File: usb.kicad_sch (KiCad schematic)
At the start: 67 parts, among them J3 USB-C_GCT_USB4105-GF-A, Q2 BC817-25W, U11 AP22652W6, U2 FT4232H_VQFN, U4 AP62301_TSOT, U5 TPD4E05U06QDQARQ1, U8 AP62301_TSOT, Y1 Resonator_12MHz_ABM8G

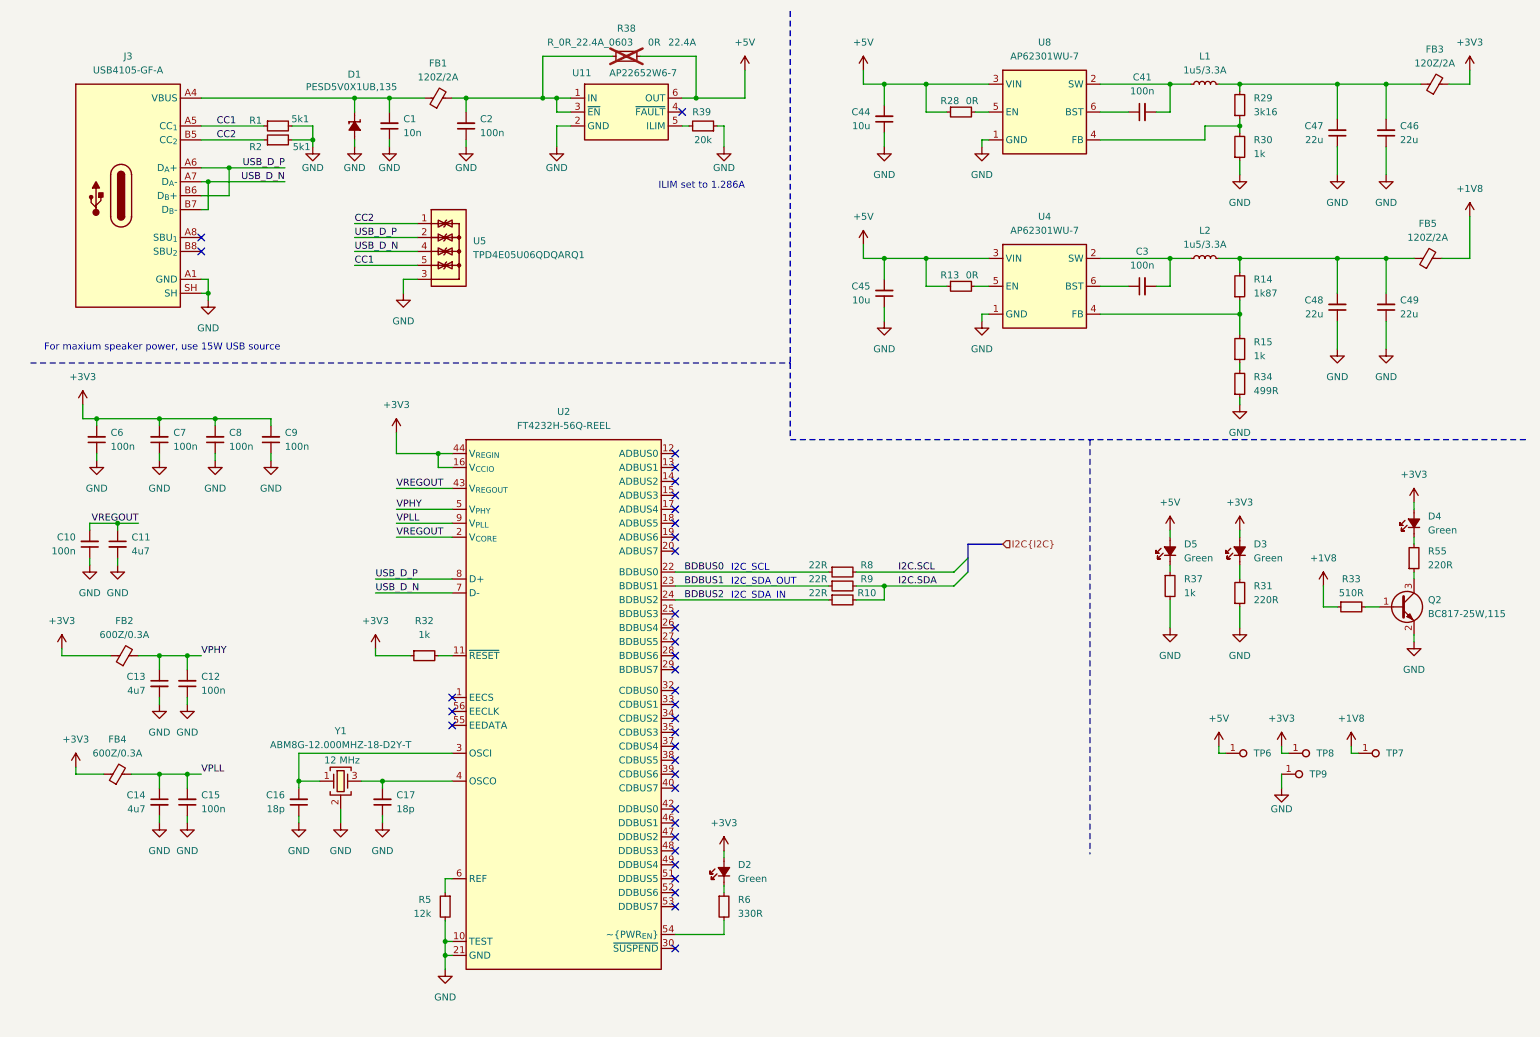
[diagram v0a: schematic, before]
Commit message: [#71555] Add new root sheet structure
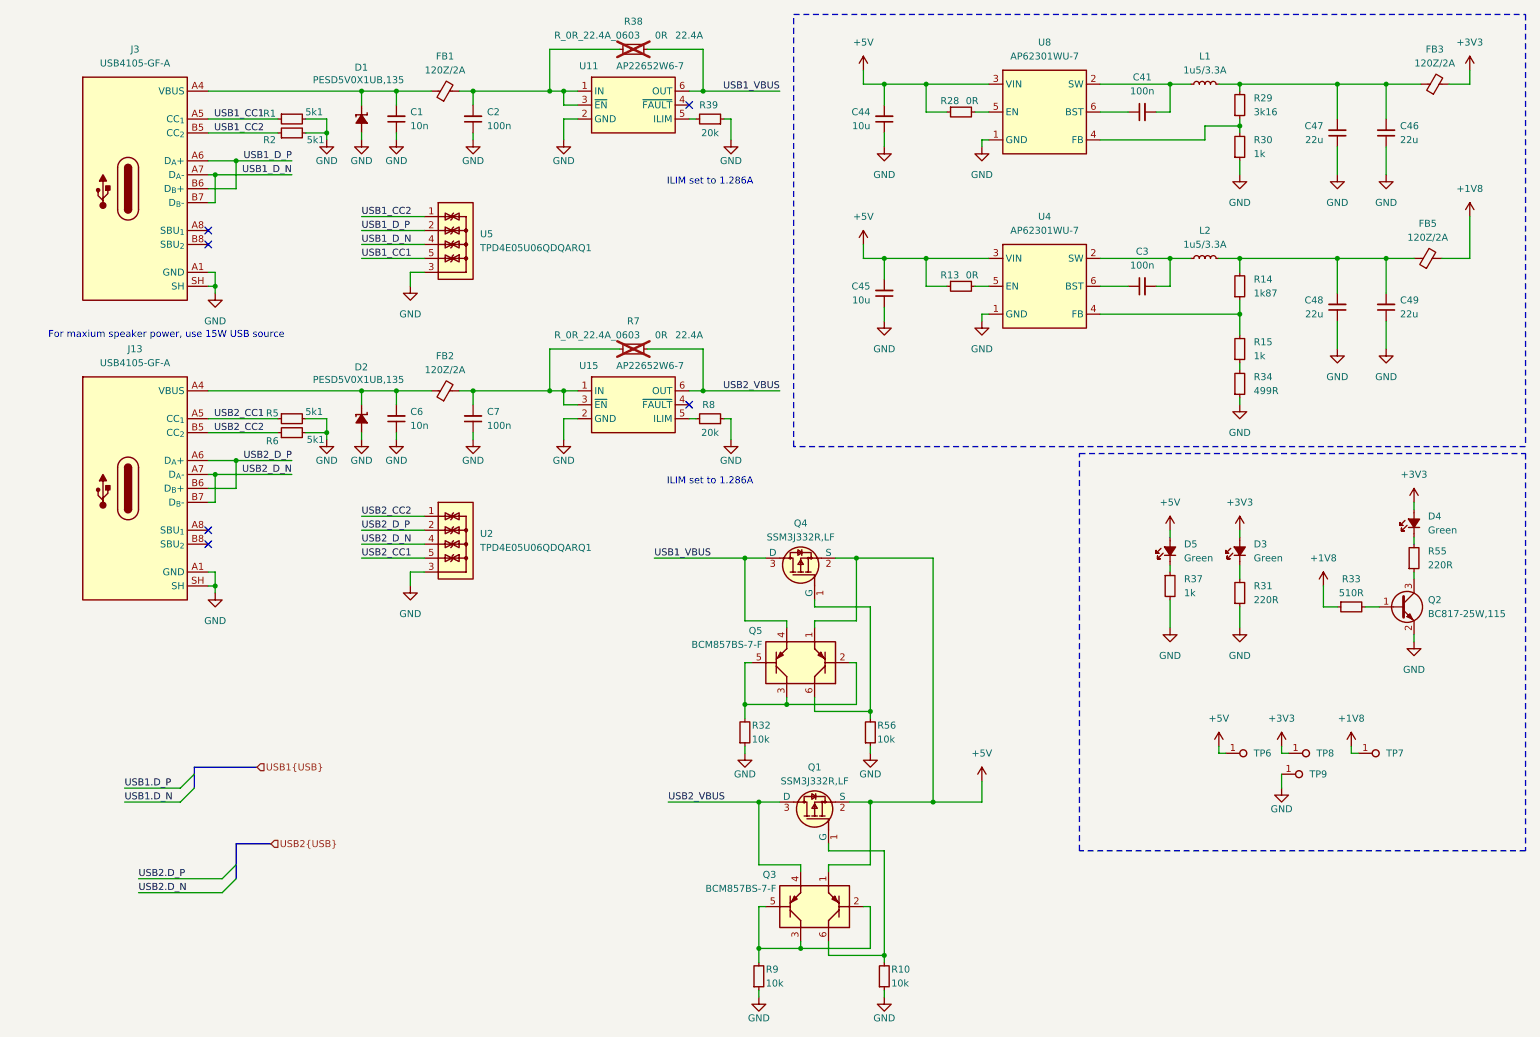
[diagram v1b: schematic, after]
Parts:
- removed C10, C12, C15, C6, C8, C9: C_100n_0402, antmicro-footprints:C_0402_1005Metric, symbol antmicroCapacitors0402:C_100n_0402
- removed C11, C13, C14: C_4u7_0402, antmicro-footprints:C_0402_1005Metric, symbol antmicroCapacitors0402:C_4u7_0402
- removed C16, C17: C_18p_0402, antmicro-footprints:C_0402_1005Metric, symbol antmicroCapacitors0402:C_18p_0402
- removed D2: LED_G_0402_VLMTG1500-GS08, antmicro-footprints:LED_0402_1005Metric_G, symbol antmicroLEDIndicationDiscrete:LED_G_0402_VLMTG1500-GS08
- removed FB2, FB4: FB_600Z_0.3A_Murata-BLM15AG_0402, antmicro-footprints:FB_0402_1005Metric, symbol antmicroFerriteBeadsandChips:FB_600Z_0.3A_Murata-BLM15AG_0402
- removed R10, R8, R9: R_22R_0402, antmicro-footprints:R_0402_1005Metric, symbol antmicroResistors0402:R_22R_0402
- removed R32: R_1k_0402, antmicro-footprints:R_0402_1005Metric, symbol antmicroResistors0402:R_1k_0402
- removed R5: R_12k_0402, antmicro-footprints:R_0402_1005Metric, symbol antmicroResistors0402:R_12k_0402
- removed R6: R_330R_0402, antmicro-footprints:R_0402_1005Metric, symbol antmicroResistors0402:R_330R_0402
- removed U2: FT4232H_VQFN, antmicro-footprints:QFN-56-1EP_8x8mm_P0.5mm, symbol antmicroInterfaceControllers:FT4232H_VQFN
- removed Y1: Resonator_12MHz_ABM8G, antmicro-footprints:Resonator_SMD_Abracon_ABM8G_3.2x2.5mm, symbol antmicroResonators:Resonator_12MHz_ABM8G
- added C6: C_10n_0402, antmicro-footprints:C_0402_1005Metric, symbol antmicroCapacitors0402:C_10n_0402
- added D2: PESD5V0X1UB, antmicro-footprints:SOD-523, symbol antmicroTVSDiodes:PESD5V0X1UB
- added FB2: FB_120Z_2A_Murata-BLM18PG_0603, antmicro-footprints:FB_0603_1608Metric, symbol antmicroFerriteBeadsandChips:FB_120Z_2A_Murata-BLM18PG_0603
- added J13: USB-C_GCT_USB4105-GF-A, antmicro-footprints:USB-C_Receptacle_GCT_USB4105-GF-A, symbol antmicroUSBConnectors:USB-C_GCT_USB4105-GF-A
- added Q1, Q4: SSM3J332R, antmicro-footprints:SOT-23-3, symbol antmicroTransistorsFETsMOSFETsSingle:SSM3J332R
- added Q3, Q5: BCM857BS-7-F, antmicro-footprints:SOT-363, symbol antmicroTransistorsBipolarArrays:BCM857BS-7-F
- added R10, R32, R56, R9: R_10k_0402, antmicro-footprints:R_0402_1005Metric, symbol antmicroResistors0402:R_10k_0402
- added R5, R6: R_5k1_0402, antmicro-footprints:R_0402_1005Metric, symbol antmicroResistors0402:R_5k1_0402
- added R7: R_0R_22.4A_0603, antmicro-footprints:R_0603_1608Metric, symbol antmicroResistors0603:R_0R_22.4A_0603
- added R8: R_20k_0402, antmicro-footprints:R_0402_1005Metric, symbol antmicroResistors0402:R_20k_0402
- added U15: AP22652W6, antmicro-footprints:SOT-23-6, symbol antmicroPMICPowerDistributionSwitchesLoadDrivers:AP22652W6
- added U2: TPD4E05U06QDQARQ1, antmicro-footprints:USON-10_2.5x1mm_P0.5mm, symbol antmicroTVSDiodes:TPD4E05U06QDQARQ1
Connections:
- net +3V3: no longer C7.2
- net +5V: now also Q1.2 (S), Q3.1, Q4.2 (S), Q5.1; no longer R38.2, U11.6 (OUT)
- net GND: now also C6.1, D2.2 (A), J13.A1 (GND), J13.A12 (GND), J13.B1 (GND), J13.B12 (GND), J13.SH, R10.1, R32.1, R5.2, R56.1, R6.2, R8.1, R9.1, U15.2 (GND), U2.3, U2.8
- net CC1 renamed USB1_CC1
- net CC2 renamed USB1_CC2
- net USB_D_N renamed USB1_D_N
- net USB_D_P renamed USB1_D_P
- new net: C6.2, D2.1 (C), FB2.1, J13.A4 (VBUS), J13.A9 (VBUS), J13.B4 (VBUS), J13.B9 (VBUS)
- new net: C7.2, FB2.2, R7.1, U15.1 (IN), U15.3 (~{EN})
- new net: Q3.2, Q3.3, Q3.5, R9.2
- new net: Q1.1 (G), Q3.6, R10.2
- new net: R8.2, U15.5 (ILIM)
- new net: Q4.1 (G), Q5.6, R56.2
- new net: Q5.2, Q5.3, Q5.5, R32.2
- new net USB1_VBUS: Q4.3 (D), Q5.4, R38.2, U11.6 (OUT)
- new net USB2_CC1: J13.A5 (CC_{1}), R5.1, U2.5, U2.6
- new net USB2_CC2: J13.B5 (CC_{2}), R6.1, U2.1, U2.10
- new net USB2_D_N: J13.A7 (D_{A}-), J13.B7 (D_{B}-), U2.4, U2.7
- new net USB2_D_P: J13.A6 (D_{A}+), J13.B6 (D_{B}+), U2.2, U2.9
- new net USB2_VBUS: Q1.3 (D), Q3.4, R7.2, U15.6 (OUT)
- no-connect marks 36 -> 6
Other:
- note removed: "I2C_SCL"
- note removed: "I2C_SDA_IN"
- note removed: "I2C_SDA_OUT"
- moved on the sheet: C1, C2, D1, FB1, J3, R1, R2, R38, R39, U11, U5

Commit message: [#71555] Draw MIC and USB Connector sheets
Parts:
- removed TP6, TP7, TP8, TP9: TP_1.5mm_SMD, antmicro-footprints:TP_SMD_1.5mm, symbol antmicroTestPoints:TP_1.5mm_SMD
- added TP1, TP2, TP3, TP4, TP5, TP6, TP7: TP_0.75mm_SMD, antmicro-footprints:TP_SMD_0.75mm, symbol antmicroTestPoints:TP_0.75mm_SMD
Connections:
- net +1V8: now also TP4.1
- net +3V3: now also TP3.1
- net +5V: now also TP2.1
- net GND: now also TP5.1
- net USB1_VBUS: now also TP6.1
- net USB2_VBUS: now also TP7.1
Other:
- note removed: "For maxium speaker power, use 15W USB source"
- moved on the sheet: C3, C41, C44, C45, C46, C47, C48, C49, C6, C7, D2, D3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

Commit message: [#71555] Prepare sch for AMP
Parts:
- added TP16, TP17: TP_0.75mm_SMD, antmicro-footprints:TP_SMD_0.75mm, symbol antmicroTestPoints:TP_0.75mm_SMD
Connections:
- net at C1.2, D1.1 (C), FB1.1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: now also TP16.1
- net at C6.2, D2.1 (C), FB2.1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: now also TP17.1

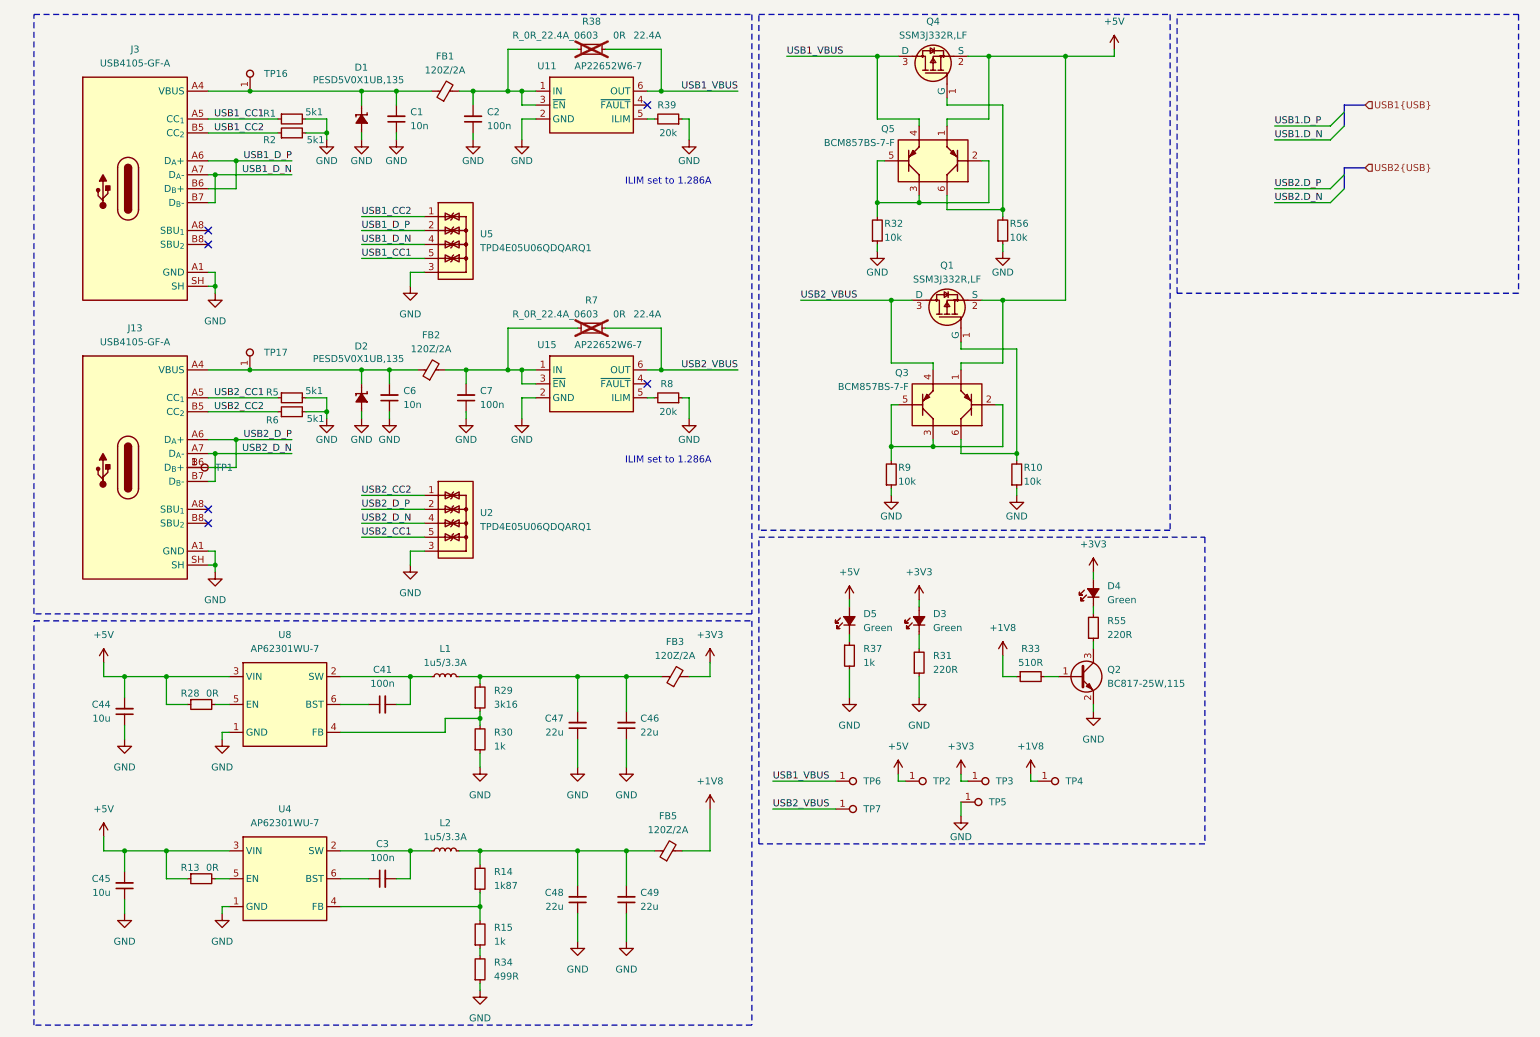
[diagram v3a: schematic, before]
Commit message: [#71555] Add connections between RP2040s
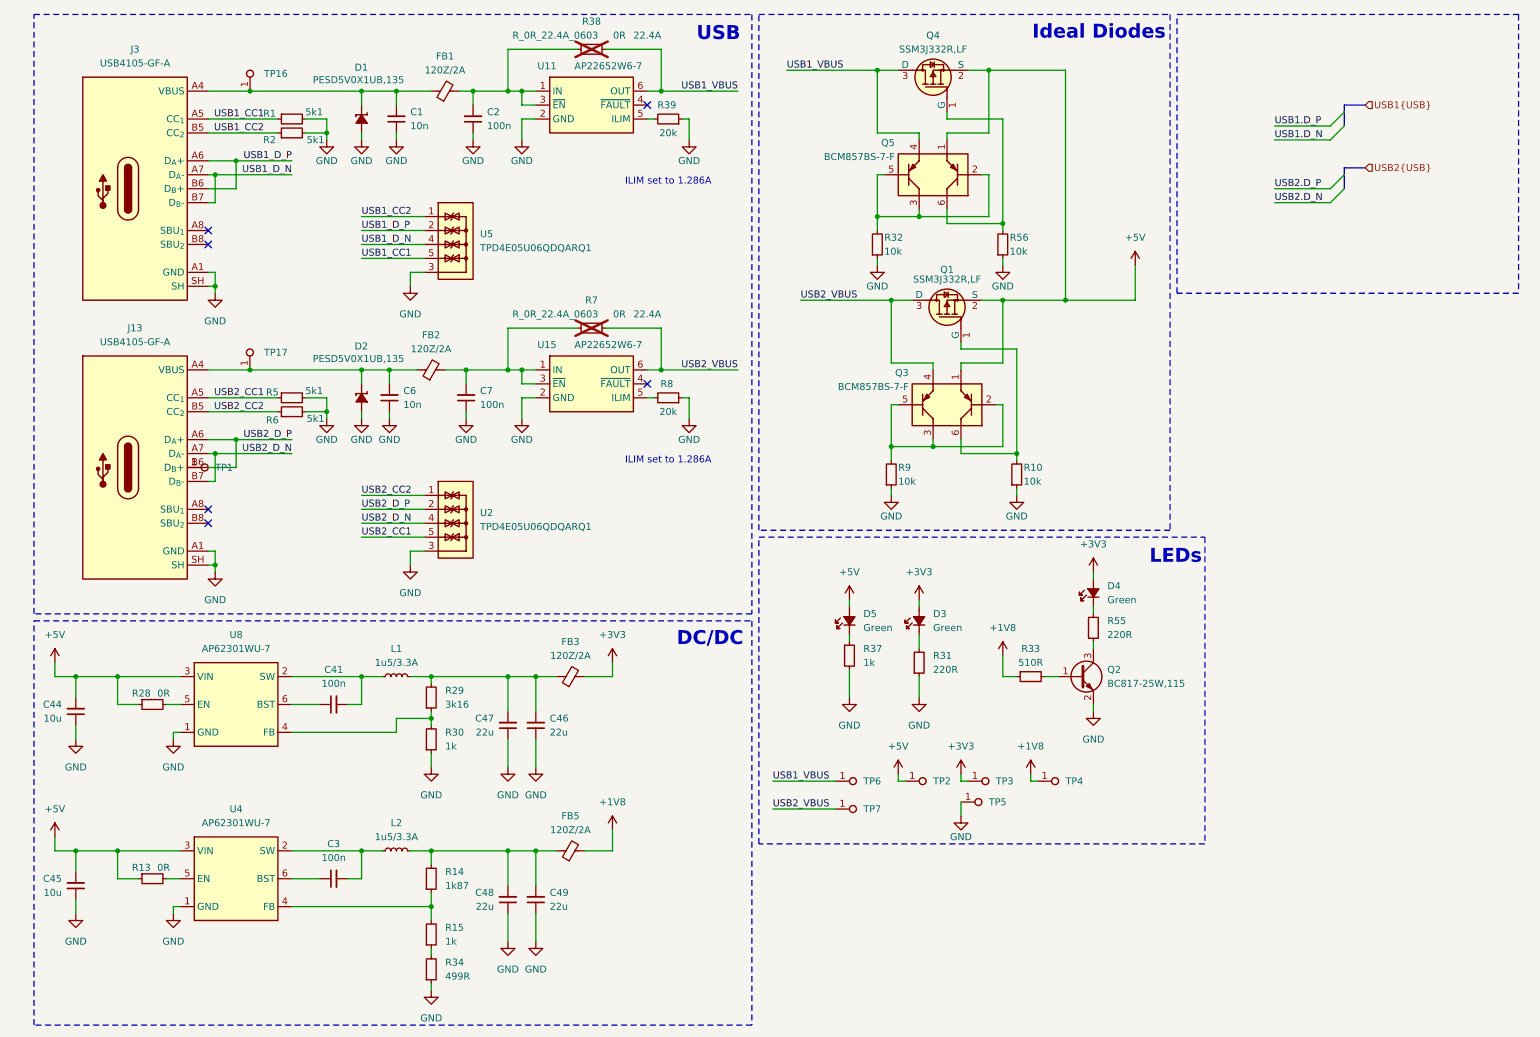
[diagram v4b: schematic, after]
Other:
- note added: "DC/DC"
- note added: "Ideal Diodes"
- note added: "LEDs"
- note added: "USB"
- moved on the sheet: C3, C41, C44, C45, C46, C47, C48, C49, FB3, FB5, L1, L2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

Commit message: [#71555] Resolve ERC
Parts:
- removed TP1: TP_0.75mm_SMD, antmicro-footprints:TP_SMD_0.75mm, symbol antmicroTestPoints:TP_0.75mm_SMD
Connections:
- net USB1.D_N: now also J3.A7 (D_{A}-), J3.B7 (D_{B}-)
- net USB1.D_P: now also J3.A6 (D_{A}+), J3.B6 (D_{B}+)
- net USB1_D_N: no longer J3.A7 (D_{A}-), J3.B7 (D_{B}-)
- net USB1_D_P: no longer J3.A6 (D_{A}+), J3.B6 (D_{B}+)
- net USB2.D_N: now also J13.A7 (D_{A}-), J13.B7 (D_{B}-)
- net USB2.D_P: now also J13.A6 (D_{A}+), J13.B6 (D_{B}+)
- net USB2_D_N: no longer J13.A7 (D_{A}-), J13.B7 (D_{B}-)
- net USB2_D_P: no longer J13.A6 (D_{A}+), J13.B6 (D_{B}+)
